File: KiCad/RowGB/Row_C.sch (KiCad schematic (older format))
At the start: 37 parts, among them U301 RGB_WS2811, U302 RGB_WS2811, U303 RGB_WS2811, U304 RGB_WS2811, U305 RGB_WS2811, U306 RGB_WS2811, U307 RGB_WS2811, U308 RGB_WS2811, U309 RGB_WS2811, U310 RGB_WS2811, U311 RGB_WS2811, U312 RGB_WS2811, U313 RGB_WS2811, U314 RGB_WS2811, U315 RGB_WS2811, U316 RGB_WS2811

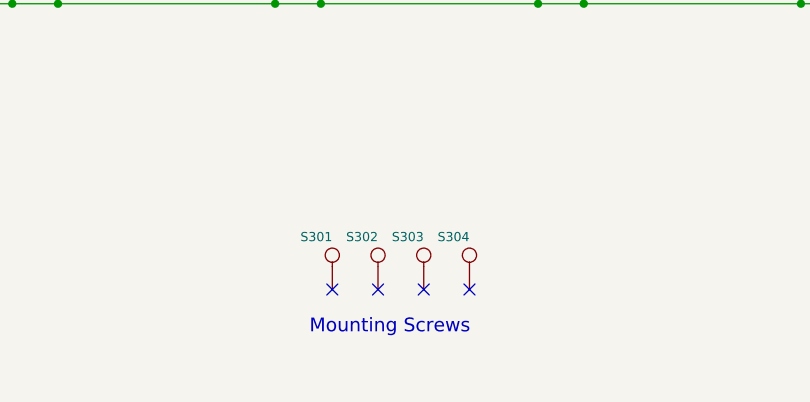
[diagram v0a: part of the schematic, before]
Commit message: TiM : Need to add legend for stacking connectors.
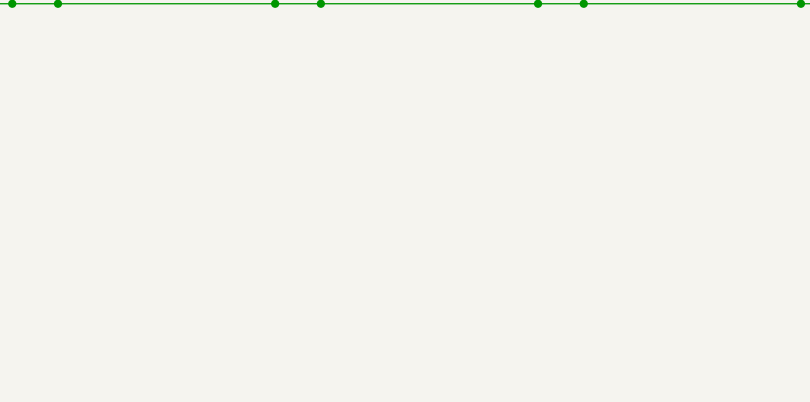
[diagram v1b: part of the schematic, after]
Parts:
- removed S301, S302, S303, S304: CONN_1, Screw, symbol CONN_1
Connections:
- no-connect marks 20 -> 16
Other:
- note removed: "Mounting Screws"
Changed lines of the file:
@@
-EESchema Schematic File Version 2  date Tuesday 12 February 2013 12:06:40 AM IST
+EESchema Schematic File Version 2  date 2/13/2013 1:59:50 PM
 LIBS:RowGB_sym
 LIBS:power
@@
 Sheet 7 9
 Title "TiM - The Intelligent Matrix"
-Date "11 feb 2013"
+Date "13 feb 2013"
 Rev ""
 Comp "WyoLum"
@@
 	1    0    0    -1
 $EndComp
-$Comp
-L CONN_1 S301
-U 1 1 5118AB79
-P 5300 6650
-F 0 "S301" V 5380 6650 40  0000 L CNN
-F 1 "CONN_1" H 5300 6705 30  0001 C CNN
-F 2 "Screw" H 5300 6805 30  0001 C CNN
-	1    5300 6650
-	0    -1   -1   0
-$EndComp
-$Comp
-L CONN_1 S302
-U 1 1 5118AB73
-P 5500 6650
-F 0 "S302" V 5580 6650 40  0000 L CNN
-F 1 "CONN_1" H 5500 6705 30  0001 C CNN
-F 2 "Screw" H 5500 6805 30  0001 C CNN
-	1    5500 6650
-	0    -1   -1   0
-$EndComp
-$Comp
-L CONN_1 S303
-U 1 1 5118AB6D
-P 5700 6650
-F 0 "S303" V 5780 6650 40  0000 L CNN
-F 1 "CONN_1" H 5700 6705 30  0001 C CNN
-F 2 "Screw" H 5700 6805 30  0001 C CNN
-	1    5700 6650
-	0    -1   -1   0
-$EndComp
-$Comp
-L CONN_1 S304
-U 1 1 5118AB67
-P 5900 6650
-F 0 "S304" V 5980 6650 40  0000 L CNN
-F 1 "CONN_1" H 5900 6705 30  0001 C CNN
-F 2 "Screw" H 5900 6805 30  0001 C CNN
-	1    5900 6650
-	0    -1   -1   0
-$EndComp
-NoConn ~ 5300 6800
-NoConn ~ 5500 6800
-NoConn ~ 5700 6800
-NoConn ~ 5900 6800
-Text Notes 5200 7000 0    60   ~ 0
-Mounting Screws
 Text Label 1250 6350 0    60   ~ 0
 5V
